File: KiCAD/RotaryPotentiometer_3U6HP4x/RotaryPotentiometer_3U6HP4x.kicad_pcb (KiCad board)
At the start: 2 copper layers, 30 x 128.5 mm, 12 parts, among them J1 Conn_01x03_Socket, J2 Conn_01x03_Socket, J3 Conn_01x03_Socket, J4 Conn_01x03_Socket

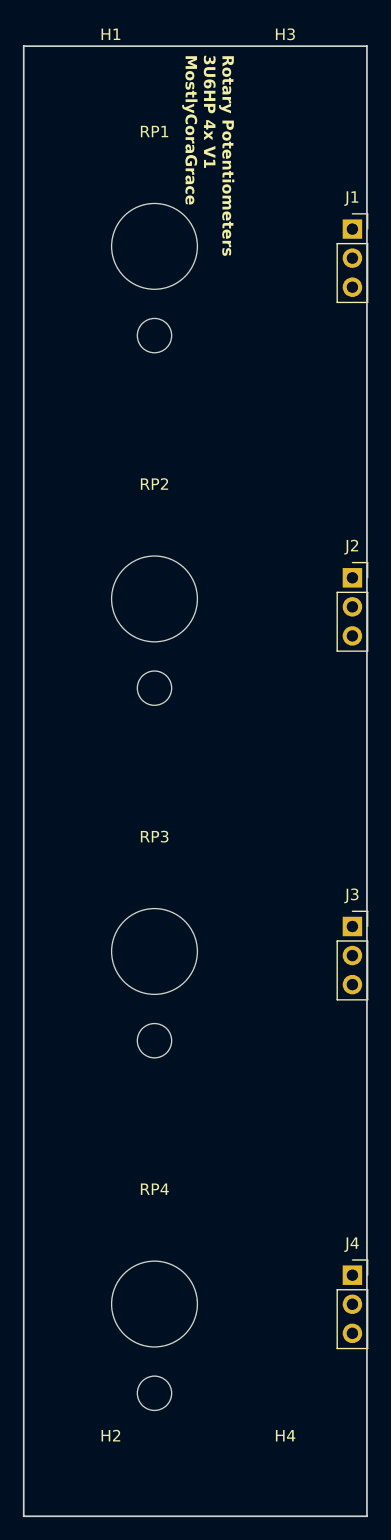
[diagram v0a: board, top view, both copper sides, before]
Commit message: removed all front silkscreen, and flipped most modules, to make the boards 'cleaner'.
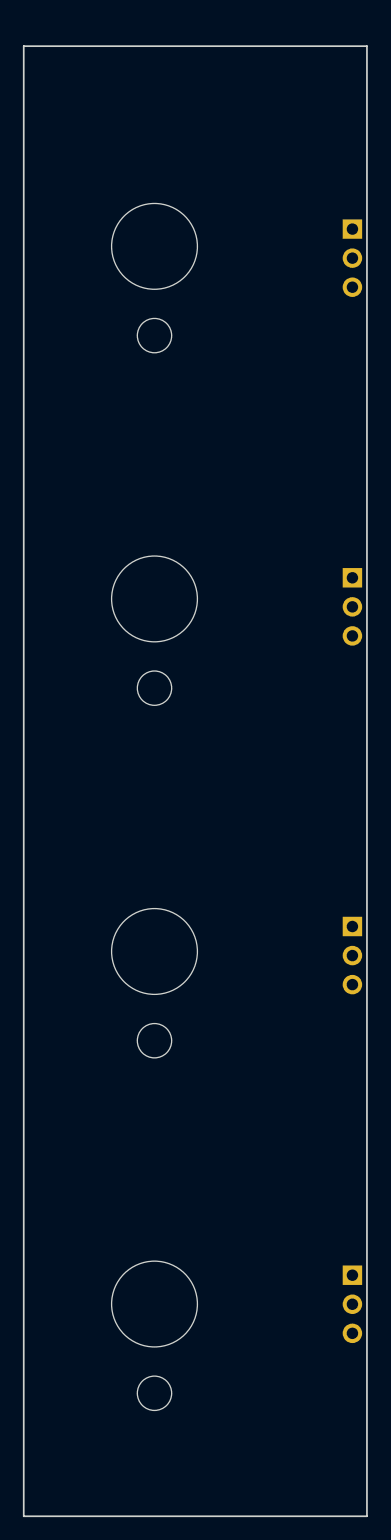
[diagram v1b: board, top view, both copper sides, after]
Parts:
- H1, H2, H3, H4, J1, J2, J3, J4: moved to B.Cu
- turned H1 to 180 degrees
- turned H2 to 180 degrees
- turned H3 to 180 degrees
- turned H4 to 180 degrees
- turned J1 to 180 degrees
- turned J2 to 180 degrees
- turned J3 to 180 degrees
- turned J4 to 180 degrees

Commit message: added copper fills to every module, to maybe possibly increase structural rigidity.
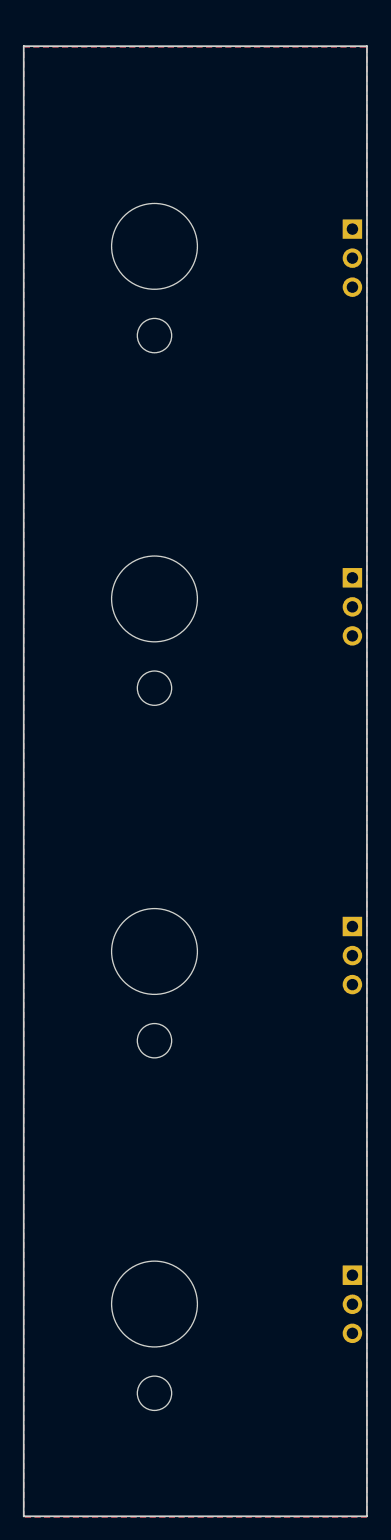
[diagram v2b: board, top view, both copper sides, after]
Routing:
- added copper zone on B.Cu, net (none)
- added copper zone on F.Cu, net (none)
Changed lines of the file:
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@@
 		(at 11.43 112.375)
 		(property "Reference" "RP4"
-			(at 0 -10 -0)
+			(at 0 -10 0)
 			(unlocked yes)
 			(layer "B.SilkS")
@@
 		)
 		(fp_text user "${REFERENCE}"
-			(at 0 -10 -0)
+			(at 0 -10 0)
 			(unlocked yes)
 			(layer "B.Fab")
@@
 		(at 11.43 81.5583)
 		(property "Reference" "RP3"
-			(at 0 -10 -0)
+			(at 0 -10 0)
 			(unlocked yes)
 			(layer "B.SilkS")
@@
 		)
 		(fp_text user "${REFERENCE}"
-			(at 0 -10 -0)
+			(at 0 -10 0)
 			(unlocked yes)
 			(layer "B.Fab")
@@
 		(at 11.43 50.7417)
 		(property "Reference" "RP2"
-			(at 0 -10 -0)
+			(at 0 -10 0)
 			(unlocked yes)
 			(layer "B.SilkS")
@@
 		)
 		(fp_text user "${REFERENCE}"
-			(at 0 -10 -0)
+			(at 0 -10 0)
 			(unlocked yes)
 			(layer "B.Fab")
@@
 		(at 11.43 19.925)
 		(property "Reference" "RP1"
-			(at 0 -10 -0)
+			(at 0 -10 0)
 			(unlocked yes)
 			(layer "B.SilkS")
@@
 		)
 		(fp_text user "${REFERENCE}"
-			(at 0 -10 -0)
+			(at 0 -10 0)
 			(unlocked yes)
 			(layer "B.Fab")
@@
 		)
 	)
+	(zone
+		(net 0)
+		(net_name "")
+		(layers "F&B.Cu")
+		(hatch edge 0.5)
+		(connect_pads
+			(clearance 0.5)
+		)
+		(min_thickness 0.25)
+		(filled_areas_thickness no)
+		(fill yes
+			(thermal_gap 0.5)
+			(thermal_bridge_width 0.5)
+			(island_removal_mode 1)
+			(island_area_min 10)
+		)
+		(polygon
+			(pts
+				(xy 0 2.5) (xy 30 2.5) (xy 30 131) (xy 0 131)
+			)
+		)
+	)

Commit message: added PCBWay print identification silkscreen text to each component
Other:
- board text added: "WayWayWay"
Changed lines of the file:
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@@
+		)
+	)
+	(gr_text "WayWayWay"
+		(at 2 130 -90)
+		(layer "B.SilkS")
+		(effects
+			(font
+				(size 1 1)
+				(thickness 0.15)
+			)
+			(justify left top mirror)
 		)
 	)
